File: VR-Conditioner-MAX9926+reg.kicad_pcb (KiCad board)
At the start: 2 copper layers, 19.7 x 19.7 mm, 26 parts, among them J2 Edge, J3 8-pin header, U1 MAX9926UAEE+, U2 AMS1117CD-5.0

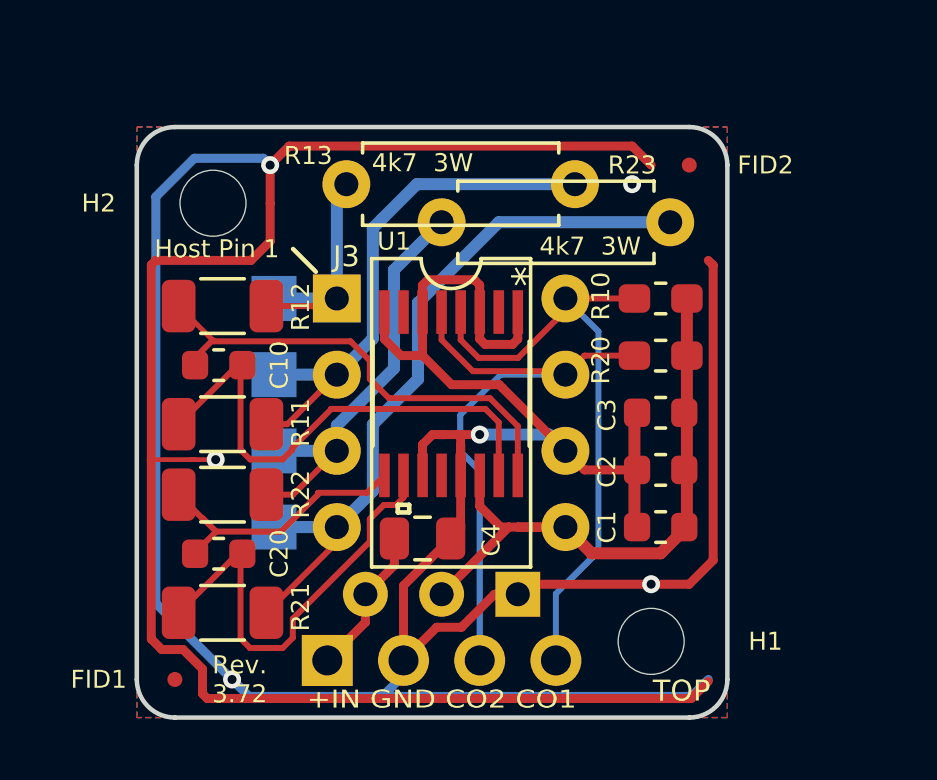
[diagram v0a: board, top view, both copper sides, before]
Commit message: v3.74 corrects channel 1 polarity, improves silkscreen & makes soldering of PTH bits easier.
Polarity in previous version not critical as everyone seems to try their pick-up each way anyhow.
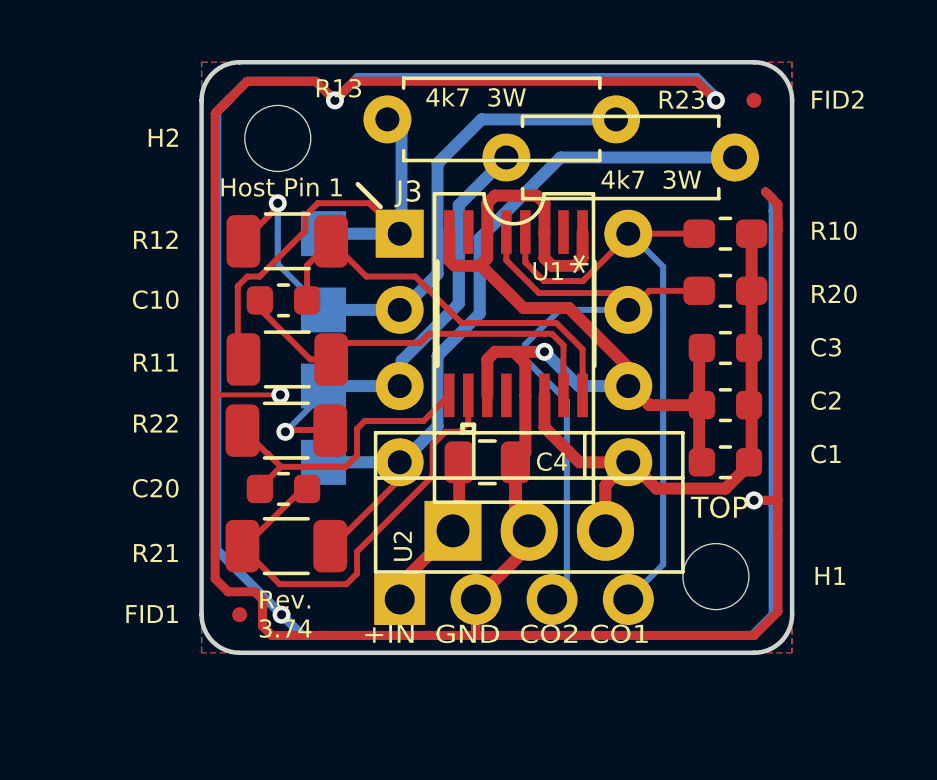
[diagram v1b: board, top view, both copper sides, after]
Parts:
- U1: value MAX9926UAEE+ -> locked
- U2: value AMS1117CD-5.0 -> L7805; footprint Package_TO_SOT_THT:TO-92_Inline_Wide -> Package_TO_SOT_THT:TO-220-3_Vertical; moved to F.Cu
- moved U1 3.43 mm to (125.0, 102.7)
- moved C4 3.33 mm to (124.1, 107.7)
- moved J2 3.15 mm to (121.2, 112.3)
- moved R21 3.08 mm to (117.4, 110.5), turned to 180 degrees
- moved C1 3.05 mm to (132.0, 107.7)
- moved C2 3.05 mm to (132.0, 105.8)
- moved C3 3.05 mm to (132.0, 103.9)
- moved H1 3.05 mm to (131.7, 111.5)
- moved R10 3.05 mm to (132.0, 100.1)
- moved R20 3.05 mm to (132.0, 102.0)
- moved R11 3.05 mm to (117.4, 104.3), turned to 180 degrees
- moved R12 3.05 mm to (117.4, 100.3), turned to 180 degrees
- moved C20 3.05 mm to (117.3, 108.6)
- moved FID1 3.05 mm to (115.8, 112.8)
- moved FID2 3.05 mm to (133.0, 95.6)
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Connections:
- R11 pad 2: Net-(J3-Pad2) -> Net-(J3-Pad1)
- R12 pad 2: Net-(J3-Pad1) -> Net-(J3-Pad2)
- R21 pad 1: Net-(C20-Pad1) -> Net-(J3-Pad4)
- R21 pad 2: Net-(J3-Pad4) -> Net-(C20-Pad1)
- R22 pad 1: Net-(C20-Pad2) -> Net-(J3-Pad3)
- R22 pad 2: Net-(J3-Pad3) -> Net-(C20-Pad2)
- U2 pad 1: GND -> +12V
- U2 pad 2: VCC -> GND
- U2 pad 3: +12V -> VCC
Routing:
- net GND: track 155.7 -> 185.0 mm
- net Net-(J3-Pad1): track 8.49 -> 16.3 mm
- net Net-(C10-Pad2): track 18.2 -> 13.3 mm
- net VCC: track 22.5 -> 19.4 mm
- net Net-(J3-Pad2): track 17.9 -> 20.5 mm, vias 0 -> 1
- net Net-(C10-Pad1): track 16.0 -> 13.7 mm
- net /COUT1: track 22.7 -> 20.8 mm
- net Net-(J3-Pad3): track 14.1 -> 15.3 mm, vias 0 -> 1
- net /COUT2: track 20.6 -> 21.6 mm
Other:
- board text added: "8-15V"
- board text added: "Dual VR"
- board text added: "MS"
- board text added: "O G I"
- board text added: "Reg.7805"
- board text added: "Rev. 3.74"
- board text added: "SoFar: + under 20x20mm & SMT components on only one side for ‘Letter’ postage. + M2 mounting holes + Optional power resistors + Optional regulator for typical automotive power + Optional pin header for breadboard etc. + Could cut at pin header for direct PCB mount by castellation Ensure all traces are at least 0.2mm. Corrected poliarity of Ch1 input. Tidied silkscreen for better readability. Orie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"
- board text added: "conditioner"
- board text removed: "&MS"
- board text removed: "6-15V+"
- board text removed: "AMS1117CD-5.0"
- board text removed: "Dual VR conditioner"
- board text removed: "Rev. 3.72"
- board text removed: "SoFar: + under 20x20mm & SMT components on only one side for ‘Letter’ postage. + M2 mounting holes + Optional power resisotrs + Optional regulator for typical automotive power + Optional pin header for breadboard etc. + Could cut at pin header for direct PCB mount by castellation 2021-04-24: Goal: Give left 6 passive components space from the left edge & the DIP Move signal trace away from right 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"
